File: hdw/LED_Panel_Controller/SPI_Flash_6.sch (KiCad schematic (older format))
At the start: 14 parts

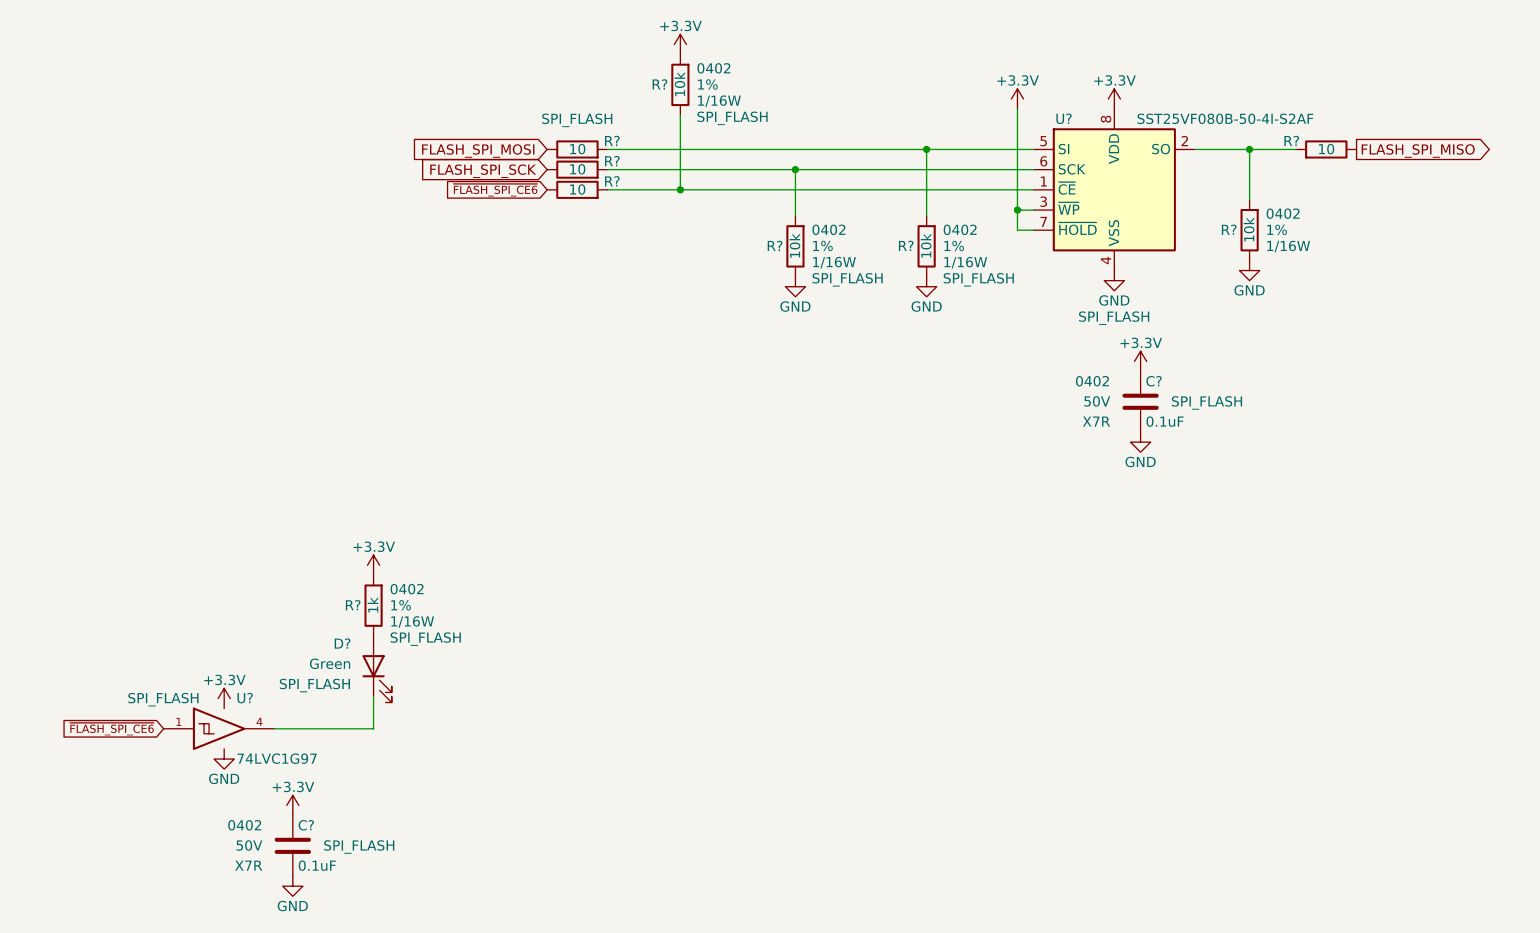
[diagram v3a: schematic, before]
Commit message: assigned I2C addresses
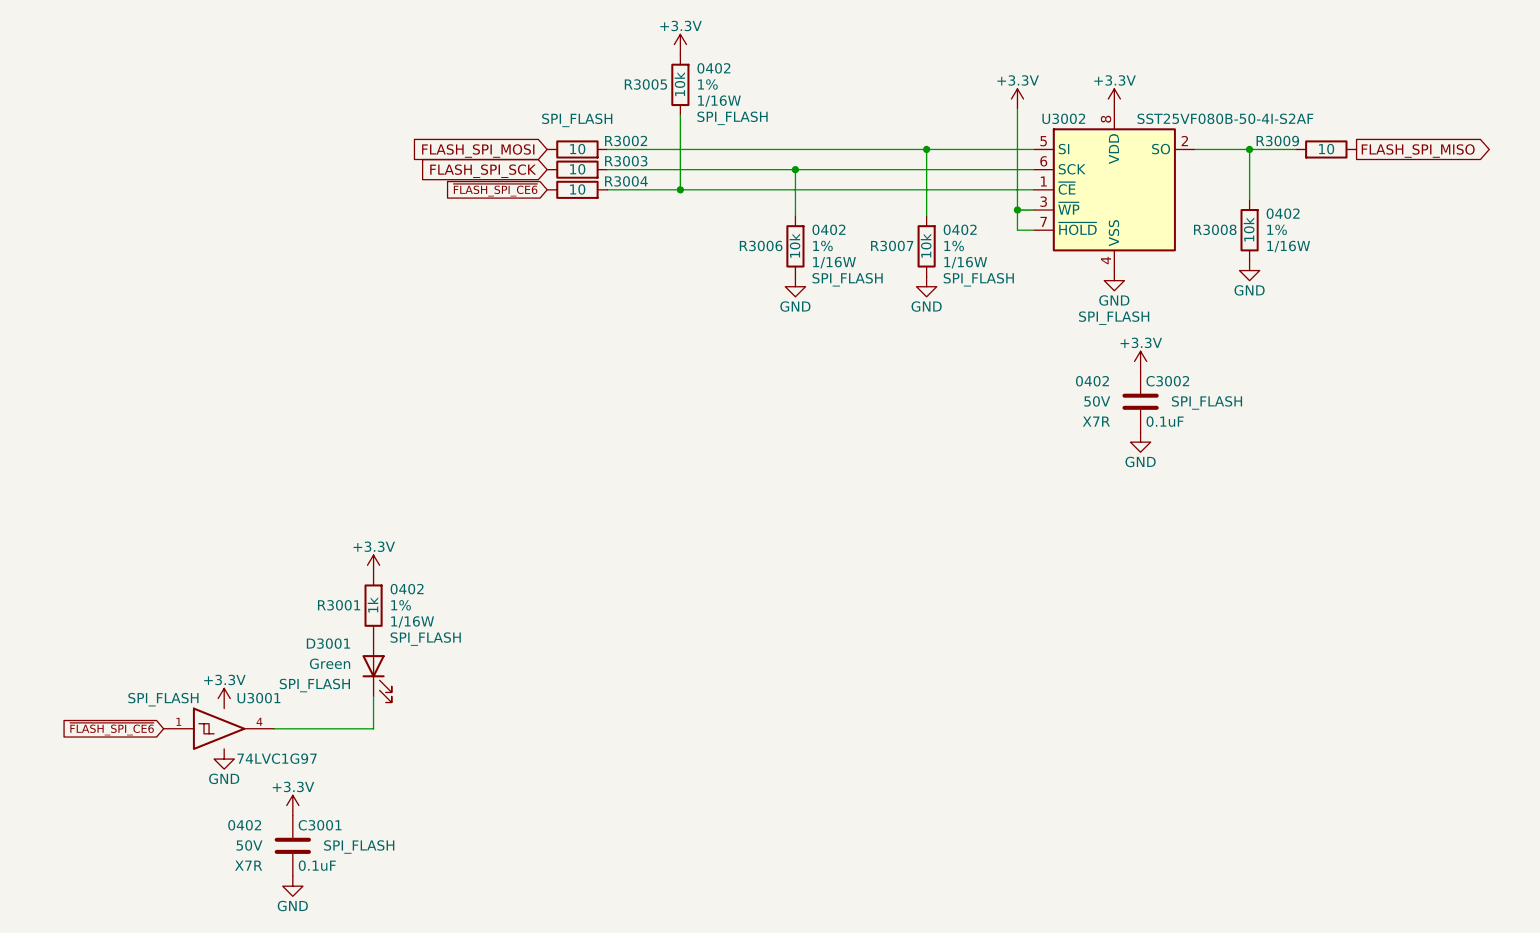
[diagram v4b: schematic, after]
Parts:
- removed C?: 0.1uF, Capacitors_SMD:C_0402, symbol Custom_Library:C_Custom
- removed D?: Green, LEDs:LED_0402, symbol Device:LED
- removed R? (x4): 10k, Resistors_SMD:R_0402, symbol Custom_Library:R_Custom
- removed R? (x4): 10, Resistors_SMD:R_0402, symbol Custom_Library:R_Custom
- removed R?: 1k, Resistors_SMD:R_0402, symbol Custom_Library:R_Custom
- removed U?: SST25VF080B-50-4I-S2AF, Package_SO:SOIC-8_5.275x5.275mm_P1.27mm, symbol Memory_Flash:SST25VF080B-50-4x-S2Ax
- removed U?: 74LVC1G97, Package_TO_SOT_SMD:SOT-363_SC-70-6, symbol Custom_Library:74LVC1G97_Power_BUF
- added C3002: 0.1uF, Capacitors_SMD:C_0402, symbol Custom_Library:C_Custom
- added D3001: Green, LEDs:LED_0402, symbol Device:LED
- added R3001: 1k, Resistors_SMD:R_0402, symbol Custom_Library:R_Custom
- added R3002, R3003, R3004, R3009: 10, Resistors_SMD:R_0402, symbol Custom_Library:R_Custom
- added R3005, R3006, R3007, R3008: 10k, Resistors_SMD:R_0402, symbol Custom_Library:R_Custom
- added U3001: 74LVC1G97, Package_TO_SOT_SMD:SOT-363_SC-70-6, symbol Custom_Library:74LVC1G97_Power_BUF
- added U3002: SST25VF080B-50-4I-S2AF, Package_SO:SOIC-8_5.275x5.275mm_P1.27mm, symbol Memory_Flash:SST25VF080B-50-4x-S2Ax
- gave numbers to parts that had none: 1
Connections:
- net +3V3: now also C3002.1, R3001.1, R3005.1, U3001.5 (VCC), U3002.3 (~WP~), U3002.7 (~HOLD~), U3002.8 (VDD)
- net FLASH_SPI_MISO: now also R3009.2
- net FLASH_SPI_MOSI: now also R3002.2
- net FLASH_SPI_SCK: now also R3003.2
- net GND: now also C3002.2, R3006.2, R3007.2, R3008.2, U3001.2 (GND), U3001.3 (GND), U3001.6 (GND), U3002.4 (VSS)
- net ~FLASH_SPI_CE6: now also R3004.2, U3001.1
- new net: R3008.1, R3009.1, U3002.2 (SO)
- new net: R3002.1, R3007.1, U3002.5 (SI)
- new net: D3001.1 (K), U3001.4
- new net: D3001.2 (A), R3001.2
- new net: R3004.1, R3005.2, U3002.1 (~CE)
- new net: R3003.1, R3006.1, U3002.6 (SCK)
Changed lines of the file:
@@
 $EndDescr
 $Comp
-L power:GND #PWR?
-U 1 1 5BB4E0E3
+L power:GND #PWR03011
+U 1 1 60786262
 P 6080 4050
-F 0 "#PWR?" H 6080 3800 50  0001 C CNN
+F 0 "#PWR03011" H 6080 3800 50  0001 C CNN
 F 1 "GND" H 6080 3900 50  0000 C CNN
 F 2 "" H 6080 4050 50  0001 C CNN
@@
 $EndComp
 $Comp
-L Custom_Library:R_Custom R?
-U 1 1 5BB4EDD1
+L Custom_Library:R_Custom R3008
+U 1 1 60786264
 P 6750 3850
-F 0 "R?" H 6690 3850 50  0000 R CNN
+F 0 "R3008" H 6690 3850 50  0000 R CNN
 F 1 "10k" V 6750 3850 50  0000 C CNN
 F 2 "Resistors_SMD:R_0402" H 6750 3850 50  0001 C CNN
@@
 $EndComp
 $Comp
-L power:GND #PWR?
-U 1 1 5BB4EE63
+L power:GND #PWR03008
+U 1 1 6078626B
 P 5150 4080
-F 0 "#PWR?" H 5150 3830 50  0001 C CNN
+F 0 "#PWR03008" H 5150 3830 50  0001 C CNN
 F 1 "GND" H 5150 3930 50  0000 C CNN
 F 2 "" H 5150 4080 50  0001 C CNN
@@
 $EndComp
 $Comp
-L power:GND #PWR?
-U 1 1 5BB4EE7C
+L power:GND #PWR03014
+U 1 1 60786272
 P 6750 4000
-F 0 "#PWR?" H 6750 3750 50  0001 C CNN
+F 0 "#PWR03014" H 6750 3750 50  0001 C CNN
 F 1 "GND" H 6750 3850 50  0000 C CNN
 F 2 "" H 6750 4000 50  0001 C CNN
@@
 $EndComp
 $Comp
-L Custom_Library:R_Custom R?
-U 1 1 5BB4F53B
+L Custom_Library:R_Custom R3002
+U 1 1 6078627C
 P 3420 3450
-F 0 "R?" V 3380 3580 50  0000 L CNN
+F 0 "R3002" V 3380 3580 50  0000 L CNN
 F 1 "10" V 3420 3450 50  0000 C CNN
 F 2 "Resistors_SMD:R_0402" H 3420 3450 50  0001 C CNN
@@
 	3570 3650 3930 3650
 $Comp
-L power:+3.3V #PWR?
-U 1 1 5BDF3D33
+L power:+3.3V #PWR03006
+U 1 1 60786280
 P 3930 2980
-F 0 "#PWR?" H 3930 2830 50  0001 C CNN
+F 0 "#PWR03006" H 3930 2830 50  0001 C CNN
 F 1 "+3.3V" H 3930 3120 50  0000 C CNN
 F 2 "" H 3930 2980 50  0001 C CNN
@@
 $EndComp
 $Comp
-L power:+3.3V #PWR?
-U 1 1 5BDF3DF4
+L power:+3.3V #PWR03010
+U 1 1 60786287
 P 6080 3250
-F 0 "#PWR?" H 6080 3100 50  0001 C CNN
+F 0 "#PWR03010" H 6080 3100 50  0001 C CNN
 F 1 "+3.3V" H 6080 3390 50  0000 C CNN
 F 2 "" H 6080 3250 50  0001 C CNN
@@
 AR Path="/5BB2595E/5C15F697" Ref="C?"  Part="1"
 AR Path="/5F583577/5C15F697" Ref="C?"  Part="1"
-AR Path="/5F5835AA/5C15F697" Ref="C?"  Part="1"
-F 0 "C?" H 2035 7000 50  0000 L CNN
+AR Path="/5F5835AA/5C15F697" Ref="C3001"  Part="1"
+F 0 "C3001" H 2035 7000 50  0000 L CNN
 F 1 "0.1uF" H 2035 6800 50  0000 L CNN
 F 2 "Capacitors_SMD:C_0402" H 2048 6750 50  0001 C CNN
@@
 $EndComp
 $Comp
-L power:+3.3V #PWR?
+L power:+3.3V #PWR03001
 U 1 1 5C161B83
 P 1670 6220
-F 0 "#PWR?" H 1670 6070 50  0001 C CNN
+F 0 "#PWR03001" H 1670 6070 50  0001 C CNN
 F 1 "+3.3V" H 1670 6360 50  0000 C CNN
 F 2 "" H 1670 6220 50  0001 C CNN
@@
 $EndComp
 $Comp
-L power:+3.3V #PWR?
-U 1 1 5C161BE9
+L power:+3.3V #PWR03003
+U 1 1 607862A1
 P 2010 6750
-F 0 "#PWR?" H 2010 6600 50  0001 C CNN
+F 0 "#PWR03003" H 2010 6600 50  0001 C CNN
 F 1 "+3.3V" H 2010 6890 50  0000 C CNN
 F 2 "" H 2010 6750 50  0001 C CNN
@@
 $EndComp
 $Comp
-L power:GND #PWR?
-U 1 1 5C161C44
+L power:GND #PWR03004
+U 1 1 607862A5
 P 2010 7050
-F 0 "#PWR?" H 2010 6800 50  0001 C CNN
+F 0 "#PWR03004" H 2010 6800 50  0001 C CNN
 F 1 "GND" H 2010 6900 50  0000 C CNN
 F 2 "" H 2010 7050 50  0001 C CNN
@@
 $EndComp
 $Comp
-L power:GND #PWR?
-U 1 1 5C161C9F
+L power:GND #PWR03002
+U 1 1 607862AC
 P 1670 6420
-F 0 "#PWR?" H 1670 6170 50  0001 C CNN
+F 0 "#PWR03002" H 1670 6170 50  0001 C CNN
 F 1 "GND" H 1670 6270 50  0000 C CNN
 F 2 "" H 1670 6420 50  0001 C CNN
@@
 $Comp
 L power:+3.3V #PWR?
-U 1 1 5C166A81
+U 1 1 607862B5
 P 2410 5560
-AR Path="/5BB844FD/5C166A81" Ref="#PWR?"  Part="1"
-AR Path="/5BF346B3/5C166A81" Ref="#PWR?"  Part="1"
-AR Path="/5BB2595E/5C166A81" Ref="#PWR?"  Part="1"
-AR Path="/5F583577/5C166A81" Ref="#PWR?"  Part="1"
-AR Path="/5F5835AA/5C166A81" Ref="#PWR?"  Part="1"
-F 0 "#PWR?" H 2410 5410 50  0001 C CNN
+AR Path="/5BB844FD/607862B5" Ref="#PWR?"  Part="1"
+AR Path="/5BF346B3/607862B5" Ref="#PWR?"  Part="1"
+AR Path="/5BB2595E/607862B5" Ref="#PWR?"  Part="1"
+AR Path="/5F583577/607862B5" Ref="#PWR?"  Part="1"
+AR Path="/5F5835AA/607862B5" Ref="#PWR03005"  Part="1"
+F 0 "#PWR03005" H 2410 5410 50  0001 C CNN
 F 1 "+3.3V" H 2410 5700 50  0000 C CNN
 F 2 "" H 2410 5560 50  0001 C CNN
@@
 $Comp
 L Device:LED D?
-U 1 1 5C166A95
+U 1 1 607862BC
 P 2410 6010
-AR Path="/5BB844FD/5C166A95" Ref="D?"  Part="1"
-AR Path="/5BF346B3/5C166A95" Ref="D?"  Part="1"
-AR Path="/5BB2595E/5C166A95" Ref="D?"  Part="1"
-AR Path="/5F583577/5C166A95" Ref="D?"  Part="1"
-AR Path="/5F5835AA/5C166A95" Ref="D?"  Part="1"
-F 0 "D?" V 2520 6120 50  0000 L CNN
+AR Path="/5BB844FD/607862BC" Ref="D?"  Part="1"
+AR Path="/5BF346B3/607862BC" Ref="D?"  Part="1"
+AR Path="/5BB2595E/607862BC" Ref="D?"  Part="1"
+AR Path="/5F583577/607862BC" Ref="D?"  Part="1"
+AR Path="/5F5835AA/607862BC" Ref="D3001"  Part="1"
+F 0 "D3001" V 2520 6120 50  0000 L CNN
 F 1 "Green" V 2420 6120 50  0000 L CNN
 F 2 "LEDs:LED_0402" H 2410 6010 50  0001 C CNN
@@
 $EndComp
 $Comp
-L Memory_Flash:SST25VF080B-50-4x-S2Ax U?
-U 1 1 5F6879D5
+L Memory_Flash:SST25VF080B-50-4x-S2Ax U3002
+U 1 1 607862F7
 P 6080 3650
-F 0 "U?" H 5830 4000 50  0000 C CNN
+F 0 "U3002" H 5830 4000 50  0000 C CNN
 F 1 "SST25VF080B-50-4I-S2AF" H 6630 4000 50  0000 C CNN
 F 2 "Package_SO:SOIC-8_5.275x5.275mm_P1.27mm" H 6080 2950 50  0001 C CNN
@@
 $EndComp
 $Comp
-L power:+3.3V #PWR?
-U 1 1 5F689292
+L power:+3.3V #PWR03012
+U 1 1 60786303
 P 6210 4550
-F 0 "#PWR?" H 6210 4400 50  0001 C CNN
+F 0 "#PWR03012" H 6210 4400 50  0001 C CNN
 F 1 "+3.3V" H 6210 4690 50  0000 C CNN
 F 2 "" H 6210 4550 50  0001 C CNN
@@
 $EndComp
 $Comp
-L power:GND #PWR?
-U 1 1 5F689298
+L power:GND #PWR03013
+U 1 1 60786308
 P 6210 4850
-F 0 "#PWR?" H 6210 4600 50  0001 C CNN
+F 0 "#PWR03013" H 6210 4600 50  0001 C CNN
 F 1 "GND" H 6210 4700 50  0000 C CNN
 F 2 "" H 6210 4850 50  0001 C CNN
@@
 $EndComp
 $Comp
-L power:+3.3V #PWR?
-U 1 1 5F69329F
+L power:+3.3V #PWR03009
+U 1 1 6078630F
 P 5600 3250
-F 0 "#PWR?" H 5600 3100 50  0001 C CNN
+F 0 "#PWR03009" H 5600 3100 50  0001 C CNN
 F 1 "+3.3V" H 5600 3390 50  0000 C CNN
 F 2 "" H 5600 3250 50  0001 C CNN
@@
 	3570 3550 4500 3550
 $Comp
-L Custom_Library:R_Custom R?
-U 1 1 5F697048
+L Custom_Library:R_Custom R3006
+U 1 1 60786313
 P 4500 3930
-F 0 "R?" H 4440 3930 50  0000 R CNN
+F 0 "R3006" H 4440 3930 50  0000 R CNN
 F 1 "10k" V 4500 3930 50  0000 C CNN
 F 2 "Resistors_SMD:R_0402" H 4500 3930 50  0001 C CNN
@@
 $EndComp
 $Comp
-L power:GND #PWR?
-U 1 1 5F697052
+L power:GND #PWR03007
+U 1 1 6078631B
 P 4500 4080
-F 0 "#PWR?" H 4500 3830 50  0001 C CNN
+F 0 "#PWR03007" H 4500 3830 50  0001 C CNN
 F 1 "GND" H 4500 3930 50  0000 C CNN
 F 2 "" H 4500 4080 50  0001 C CNN
@@
 	4500 3550 5680 3550
 $Comp
-L Custom_Library:R_Custom R?
-U 1 1 5F7379BB
+L Custom_Library:R_Custom R3003
+U 1 1 60786322
 P 3420 3550
-F 0 "R?" V 3380 3680 50  0000 L CNN
+F 0 "R3003" V 3380 3680 50  0000 L CNN
 F 1 "10" V 3420 3550 50  0000 C CNN
 F 2 "Resistors_SMD:R_0402" H 3420 3550 50  0001 C CNN
@@
 $EndComp
 $Comp
-L Custom_Library:R_Custom R?
-U 1 1 5F737B74
+L Custom_Library:R_Custom R3004
+U 1 1 60786329
 P 3420 3650
-F 0 "R?" V 3380 3780 50  0000 L CNN
+F 0 "R3004" V 3380 3780 50  0000 L CNN
 F 1 "10" V 3420 3650 50  0000 C CNN
 F 2 "Resistors_SMD:R_0402" H 3420 3650 50  0001 C CNN
@@
 $EndComp
 $Comp
-L Custom_Library:R_Custom R?
-U 1 1 5F737D15
+L Custom_Library:R_Custom R3009
+U 1 1 60786333
 P 7130 3450
-F 0 "R?" V 7090 3580 50  0000 L CNN
+F 0 "R3009" V 7090 3580 50  0000 L CNN
 F 1 "10" V 7130 3450 50  0000 C CNN
 F 2 "Resistors_SMD:R_0402" H 7130 3450 50  0001 C CNN
@@
 $EndComp
 $Comp
-L Custom_Library:74LVC1G97_Power_BUF U?
-U 1 1 5FE9D8D5
+L Custom_Library:74LVC1G97_Power_BUF U3001
+U 1 1 60786348
 P 1670 6320
-F 0 "U?" H 1730 6470 50  0000 L CNN
+F 0 "U3001" H 1730 6470 50  0000 L CNN
 F 1 "74LVC1G97" H 1730 6170 50  0000 L CNN
 F 2 "Package_TO_SOT_SMD:SOT-363_SC-70-6" H 1720 6320 50  0001 C CNN
@@
 $EndComp
 $Comp
-L Custom_Library:R_Custom R?
-U 1 1 6026393A
+L Custom_Library:R_Custom R3007
+U 1 1 6078635B
 P 5150 3930
-F 0 "R?" H 5090 3930 50  0000 R CNN
+F 0 "R3007" H 5090 3930 50  0000 R CNN
 F 1 "10k" V 5150 3930 50  0000 C CNN
 F 2 "Resistors_SMD:R_0402" H 5150 3930 50  0001 C CNN
@@
 $EndComp
 $Comp
-L Custom_Library:R_Custom R?
-U 1 1 60263FB7
+L Custom_Library:R_Custom R3005
+U 1 1 6078635F
 P 3930 3130
-F 0 "R?" H 3870 3130 50  0000 R CNN
+F 0 "R3005" H 3870 3130 50  0000 R CNN
 F 1 "10k" V 3930 3130 50  0000 C CNN
 F 2 "Resistors_SMD:R_0402" H 3930 3130 50  0001 C CNN
@@
 $EndComp
 $Comp
-L Custom_Library:R_Custom R?
-U 1 1 60266213
+L Custom_Library:R_Custom R3001
+U 1 1 60786367
 P 2410 5710
-F 0 "R?" H 2350 5710 50  0000 R CNN
+F 0 "R3001" H 2350 5710 50  0000 R CNN
 F 1 "1k" V 2410 5710 50  0000 C CNN
 F 2 "Resistors_SMD:R_0402" H 2410 5710 50  0001 C CNN
@@
 $Comp
 L Custom_Library:C_Custom C?
-U 1 1 60269564
+U 1 1 6078636F
 P 6210 4700
-AR Path="/5BAAE16C/60269564" Ref="C?"  Part="1"
-AR Path="/5BB181D8/60269564" Ref="C?"  Part="1"
-AR Path="/5BB2595E/60269564" Ref="C?"  Part="1"
-AR Path="/5F583577/60269564" Ref="C?"  Part="1"
-AR Path="/5F5835AA/60269564" Ref="C?"  Part="1"
-F 0 "C?" H 6235 4800 50  0000 L CNN
+AR Path="/5BAAE16C/6078636F" Ref="C?"  Part="1"
+AR Path="/5BB181D8/6078636F" Ref="C?"  Part="1"
+AR Path="/5BB2595E/6078636F" Ref="C?"  Part="1"
+AR Path="/5F583577/6078636F" Ref="C?"  Part="1"
+AR Path="/5F5835AA/6078636F" Ref="C3002"  Part="1"
+F 0 "C3002" H 6235 4800 50  0000 L CNN
 F 1 "0.1uF" H 6235 4600 50  0000 L CNN
 F 2 "Capacitors_SMD:C_0402" H 6248 4550 50  0001 C CNN
